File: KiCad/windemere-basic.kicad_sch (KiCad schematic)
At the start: 51 parts, among them J2 Barrel_Jack, SW1 SW_SPDT, SW2 Push_Button, U1 WD65C02, U2 28C256, U3 62256, U4 WD65C22, U5 HD44780U, U6 74HC00, U7 MM74C922, U8 L7805, X1 1MHz

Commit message: pcb
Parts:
- R7: footprint Resistor_THT:R_Axial_DIN0207_L6.3mm_D2.5mm_P10.16mm_Horizontal -> Resistor_THT:R_Axial_DIN0204_L3.6mm_D1.6mm_P7.62mm_Horizontal
- U1: footprint 6502-Build:DIP-40_6502 -> Package_DIP:DIP-40_W15.24mm
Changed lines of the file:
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@@
       (effects (font (size 1.524 1.524)))
     )
-    (property "Footprint" "6502-Build:DIP-40_6502" (id 2) (at 34.29 66.04 0)
+    (property "Footprint" "Package_DIP:DIP-40_W15.24mm" (id 2) (at 34.29 66.04 0)
       (effects (font (size 1.524 1.524)) hide)
     )
@@
       (effects (font (size 1.27 1.27)) (justify left))
     )
-    (property "Footprint" "Resistor_THT:R_Axial_DIN0207_L6.3mm_D2.5mm_P10.16mm_Horizontal" (id 2) (at 55.372 148.59 90)
+    (property "Footprint" "Resistor_THT:R_Axial_DIN0204_L3.6mm_D1.6mm_P7.62mm_Horizontal" (id 2) (at 55.372 148.59 90)
       (effects (font (size 1.27 1.27)) hide)
     )
@@
     )
     (path "/ce736e65-66e4-4a77-a33d-4fcadf989038"
-      (reference "R7") (unit 1) (value "1k") (footprint "Resistor_THT:R_Axial_DIN0207_L6.3mm_D2.5mm_P10.16mm_Horizontal")
+      (reference "R7") (unit 1) (value "1k") (footprint "Resistor_THT:R_Axial_DIN0204_L3.6mm_D1.6mm_P7.62mm_Horizontal")
     )
     (path "/147aafce-eefa-40b0-bbcc-357bc9c489cd"
@@
     )
     (path "/6139204c-53ef-44fa-93ff-2d6092722952"
-      (reference "U1") (unit 1) (value "WD65C02") (footprint "6502-Build:DIP-40_6502")
+      (reference "U1") (unit 1) (value "WD65C02") (footprint "Package_DIP:DIP-40_W15.24mm")
     )
     (path "/d218171f-2b8a-4061-9bea-fd463a7d5174"

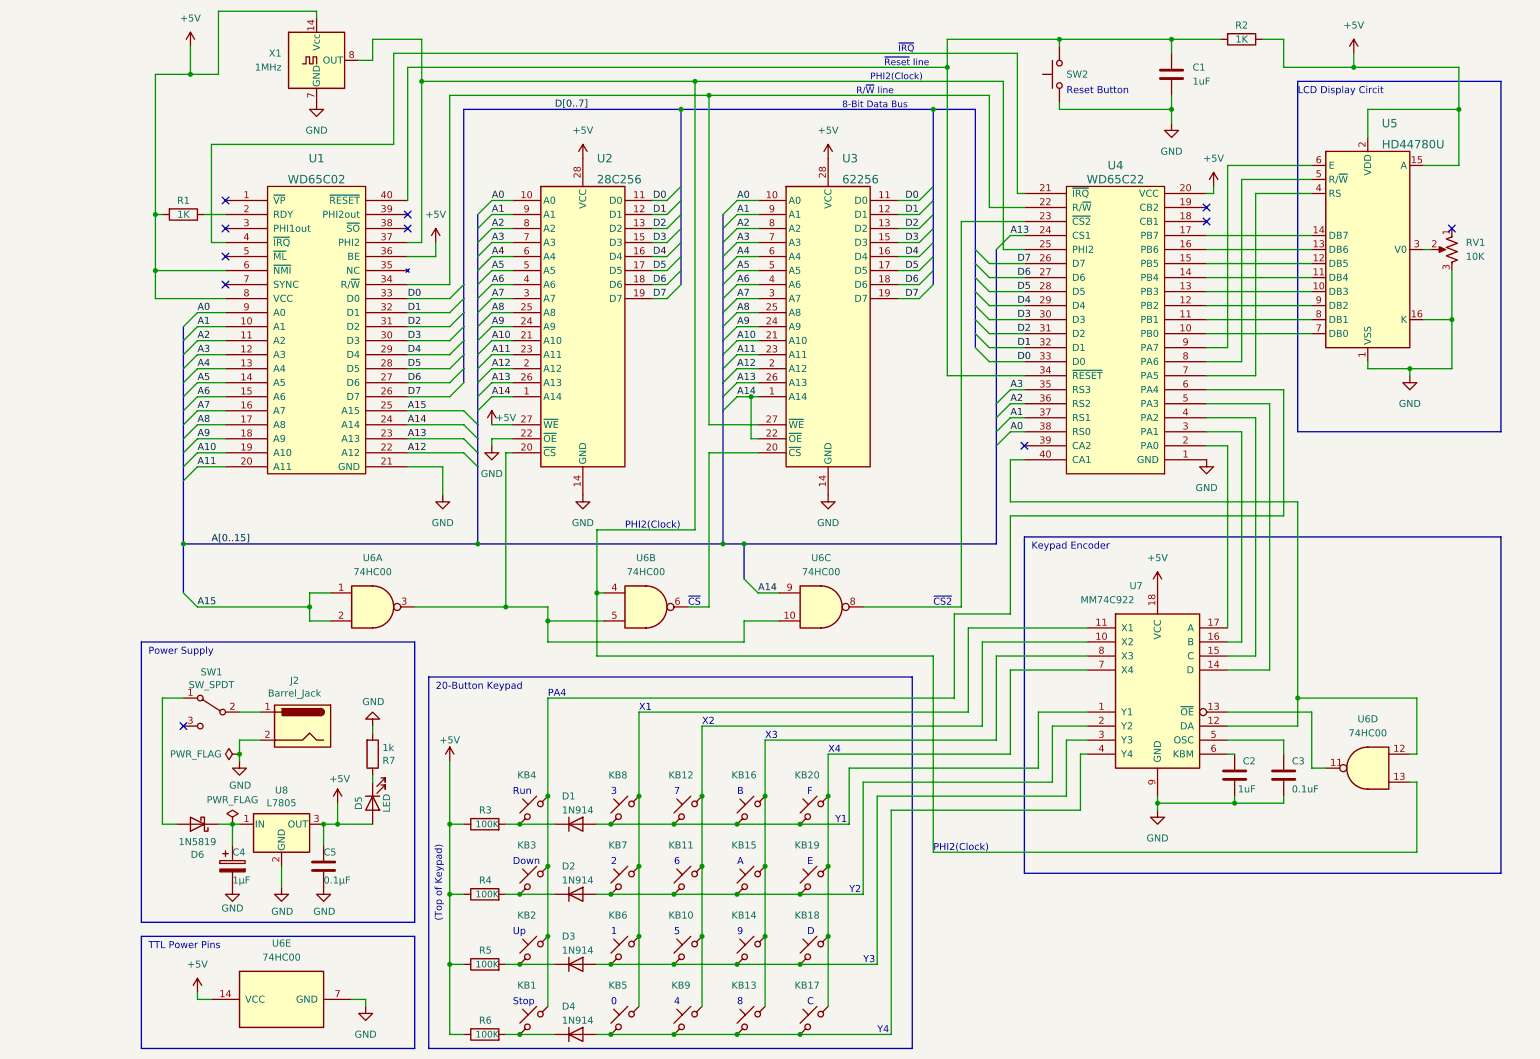
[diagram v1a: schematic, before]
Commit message: footprint updates
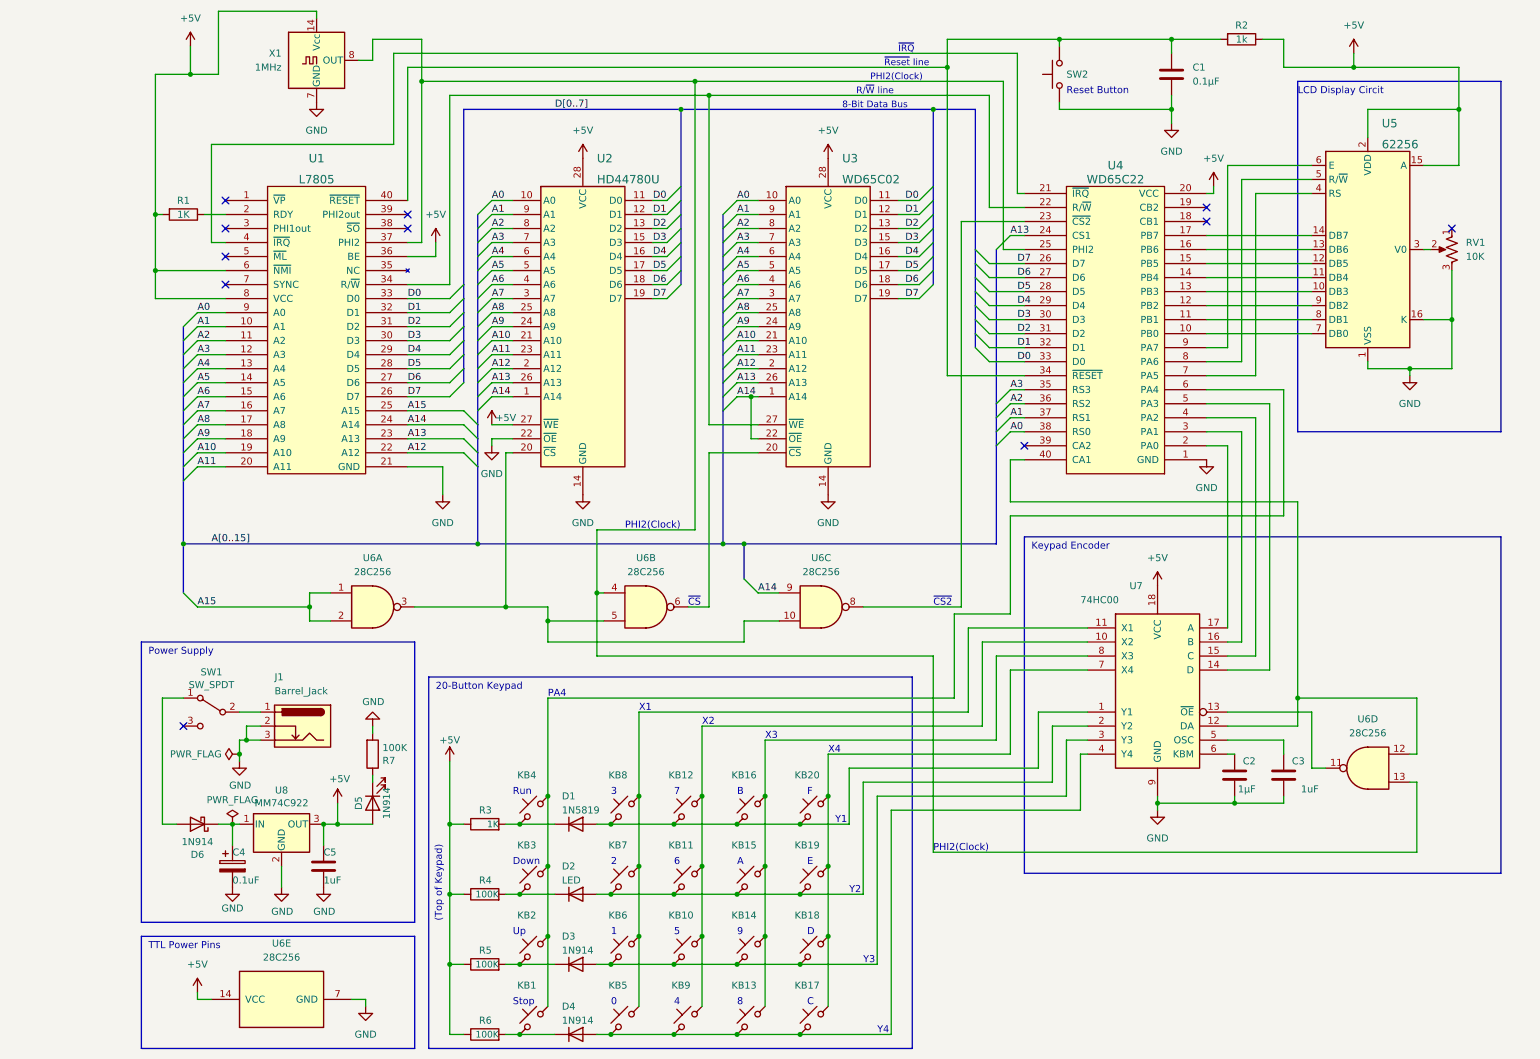
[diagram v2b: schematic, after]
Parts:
- removed J2: Barrel_Jack, Connector_BarrelJack:BarrelJack_Horizontal, symbol Connector:Barrel_Jack
- added J1: Barrel_Jack, Connector_BarrelJack:BarrelJack_Horizontal, symbol Connector:Barrel_Jack_Switch_Pin3Ring
- C1: value 1uF -> 0.1µF
- C2: value 1uF -> 1µF; footprint Capacitor_THT:C_Disc_D5.0mm_W2.5mm_P2.50mm -> Capacitor_THT:C_Radial_D4.0mm_H7.0mm_P1.50mm
- C3: value 0.1uF -> 1uF
- C4: value 1µF -> 0.1uF; footprint Capacitor_THT:C_Radial_D4.0mm_H7.0mm_P1.50mm -> Capacitor_THT:C_Disc_D5.0mm_W2.5mm_P2.50mm
- C5: value 0.1µF -> 1uF
- D1: value 1N914 -> 1N5819; footprint Diode_THT:D_DO-35_SOD27_P7.62mm_Horizontal -> Diode_THT:D_DO-41_SOD81_P10.16mm_Horizontal
- D2: value 1N914 -> LED; footprint Diode_THT:D_DO-35_SOD27_P7.62mm_Horizontal -> LED_THT:LED_D5.0mm
- D5: value LED -> 1N914; footprint LED_THT:LED_D5.0mm -> Diode_THT:D_DO-35_SOD27_P7.62mm_Horizontal
- D6: value 1N5819 -> 1N914; footprint Diode_THT:D_DO-41_SOD81_P10.16mm_Horizontal -> Diode_THT:D_DO-35_SOD27_P7.62mm_Horizontal
- R2: value 1K -> 1k
- R3: value 100K -> 1K; footprint Resistor_THT:R_Axial_DIN0207_L6.3mm_D2.5mm_P10.16mm_Horizontal -> Resistor_THT:R_Axial_DIN0204_L3.6mm_D1.6mm_P7.62mm_Horizontal
- R7: value 1k -> 100K; footprint Resistor_THT:R_Axial_DIN0204_L3.6mm_D1.6mm_P7.62mm_Horizontal -> Resistor_THT:R_Axial_DIN0207_L6.3mm_D2.5mm_P10.16mm_Horizontal
- SW1: footprint Button_Switch_THT:SW_CuK_OS102011MA1QN1_SPDT_Angled -> Button_Switch_THT:SW_CuK_JS202011CQN_DPDT_Straight
- SW2: footprint Button_Switch_THT:SW_DIP_SPSTx01_Slide_9.78x4.72mm_W7.62mm_P2.54mm -> Button_Switch_THT:SW_PUSH_6mm_H4.3mm
- U1: value WD65C02 -> L7805; footprint Package_DIP:DIP-40_W15.24mm -> Package_TO_SOT_THT:TO-220-3_Horizontal_TabDown
- U2: value 28C256 -> HD44780U; footprint Package_DIP:DIP-28_W15.24mm -> Display:WC1602A
- U3: value 62256 -> WD65C02; footprint Package_DIP:DIP-28_W15.24mm -> Package_DIP:DIP-40_W15.24mm
- U5: value HD44780U -> 62256; footprint Display:WC1602A -> Package_DIP:DIP-28_W15.24mm
- U6: value 74HC00 -> 28C256; footprint Package_DIP:DIP-14_W7.62mm -> Package_DIP:DIP-28_W15.24mm
- U7: value MM74C922 -> 74HC00; footprint Package_DIP:DIP-18_W7.62mm -> Package_DIP:DIP-14_W7.62mm
- U8: value L7805 -> MM74C922; footprint Package_TO_SOT_THT:TO-220-3_Horizontal_TabDown -> Package_DIP:DIP-18_W7.62mm
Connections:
- net GND: now also J1.2, J1.3
- net at SW1.2 (B): now also J1.1

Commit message: correct issues
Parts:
- removed C4: 0.1uF, Capacitor_THT:C_Disc_D5.0mm_W2.5mm_P2.50mm, symbol Device:CP
- removed C5: 1uF, Capacitor_THT:C_Disc_D5.0mm_W2.5mm_P2.50mm, symbol Device:C
- removed D5: 1N914, Diode_THT:D_DO-35_SOD27_P7.62mm_Horizontal, symbol Device:LED
- removed D6: 1N914, Diode_THT:D_DO-35_SOD27_P7.62mm_Horizontal, symbol Diode:1N5819
- removed J1: Barrel_Jack, Connector_BarrelJack:BarrelJack_Horizontal, symbol Connector:Barrel_Jack_Switch_Pin3Ring
- removed R7: 100K, Resistor_THT:R_Axial_DIN0207_L6.3mm_D2.5mm_P10.16mm_Horizontal, symbol Device:R
- removed SW1: SW_SPDT, Button_Switch_THT:SW_CuK_JS202011CQN_DPDT_Straight, symbol Switch:SW_SPDT
- removed unit 4 of U6
- added BZ?: Buzzer, symbol Device:Buzzer
- added C2: 0.1uF, Capacitor_THT:C_Disc_D5.0mm_W2.5mm_P2.50mm, symbol Device:C_Small
- added C5: 1µF, Capacitor_THT:C_Radial_D4.0mm_H7.0mm_P1.50mm, symbol Device:CP
- added C6: 0.1µF, Capacitor_THT:C_Disc_D5.0mm_W2.5mm_P2.50mm, symbol Device:C
- added D1: LED, LED_THT:LED_D5.0mm, symbol Device:LED
- added D2: 1N5819, Diode_THT:D_DO-41_SOD81_P10.16mm_Horizontal, symbol Diode:1N5819
- added J1: Barrel_Jack, Connector_BarrelJack:BarrelJack_Horizontal, symbol Connector:Barrel_Jack
- added R3: 1k, Resistor_THT:R_Axial_DIN0204_L3.6mm_D1.6mm_P7.62mm_Horizontal, symbol Device:R
- added SW2: SW_SPDT, Button_Switch_THT:SW_E-Switch_EG1271_DPDT, symbol Switch:SW_SPDT
- C1: value 0.1µF -> 1uF
- C3: renamed from C2; value 1µF -> 1uF; footprint Capacitor_THT:C_Radial_D4.0mm_H7.0mm_P1.50mm -> Capacitor_THT:C_Disc_D5.0mm_W2.5mm_P2.50mm
- C4: renamed from C3; value 1uF -> 0.1uF
- D3: renamed from D1; value 1N5819 -> 1N914; footprint Diode_THT:D_DO-41_SOD81_P10.16mm_Horizontal -> Diode_THT:D_DO-35_SOD27_P7.62mm_Horizontal
- D4: renamed from D2; value LED -> 1N914; footprint LED_THT:LED_D5.0mm -> Diode_THT:D_DO-35_SOD27_P7.62mm_Horizontal
- R1: renamed from R2; value 1k -> 1K
- R4: renamed from R3; value 1K -> 100K; footprint Resistor_THT:R_Axial_DIN0204_L3.6mm_D1.6mm_P7.62mm_Horizontal -> Resistor_THT:R_Axial_DIN0207_L6.3mm_D2.5mm_P10.16mm_Horizontal
- SW1: renamed from SW2; footprint Button_Switch_THT:SW_PUSH_6mm_H4.3mm -> Button_Switch_THT:SW_PUSH_6mm
- U1: renamed from U5; value 62256 -> HD44780U; footprint Package_DIP:DIP-28_W15.24mm -> Display:WC1602A
- U2: renamed from U1; value L7805 -> WD65C02; footprint Package_TO_SOT_THT:TO-220-3_Horizontal_TabDown -> Package_DIP:DIP-40_W15.24mm
- U3: renamed from U2; value HD44780U -> 28C256; footprint Display:WC1602A -> Package_DIP:DIP-28_W15.24mm
- U4: renamed from U3; value WD65C02 -> 62256; footprint Package_DIP:DIP-40_W15.24mm -> Package_DIP:DIP-28_W15.24mm
- U6: value 28C256 -> 74HC00; footprint Package_DIP:DIP-28_W15.24mm -> Package_DIP:DIP-14_W7.62mm
- U7: value 74HC00 -> MM74C922; footprint Package_DIP:DIP-14_W7.62mm -> Package_DIP:DIP-18_W7.62mm
- U8: value MM74C922 -> L7805; footprint Package_DIP:DIP-18_W7.62mm -> Package_TO_SOT_THT:TO-220-3_Horizontal_TabDown
- renumbered D3 to D5, D4 to D6, KB4 to KB1, KB19 to KB10, KB2 to KB11, KB6 to KB12, KB10 to KB13, KB18 to KB15, KB1 to KB16, KB5 to KB17, KB9 to KB18, KB13 to KB19, KB8 to KB2, KB17 to KB20, KB12 to KB3, KB16 to KB4, KB20 to KB5, KB3 to KB6, KB11 to KB8, KB15 to KB9, R1 to R2, R4 to R5, R5 to R6, R6 to R7, U4 to U5
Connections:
- net +5V: now also C2.1, C6.1, D1.2 (A)
- net GND: now also U7.13 (~{OE}), BZ?.2 (+), C2.2, C5.2, C6.2, J1.2, J1.3, R3.2
- net at U8.1 (IN): now also C5.1, D2.1 (K)
- net at U5.19 (CB2): now also BZ?.1 (-)
- new net: D2.2 (A), SW2.1 (A)
- new net: J1.1, SW2.2 (B)
- new net: D1.1 (K), R3.1
- no-connect marks 11 -> 10
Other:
- title: WD65C02 Homebrew Computer Mainboard -> Windemere Basic
- moved on the sheet: C3, C4, R1, U7
